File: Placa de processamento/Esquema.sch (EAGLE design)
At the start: 14 parts

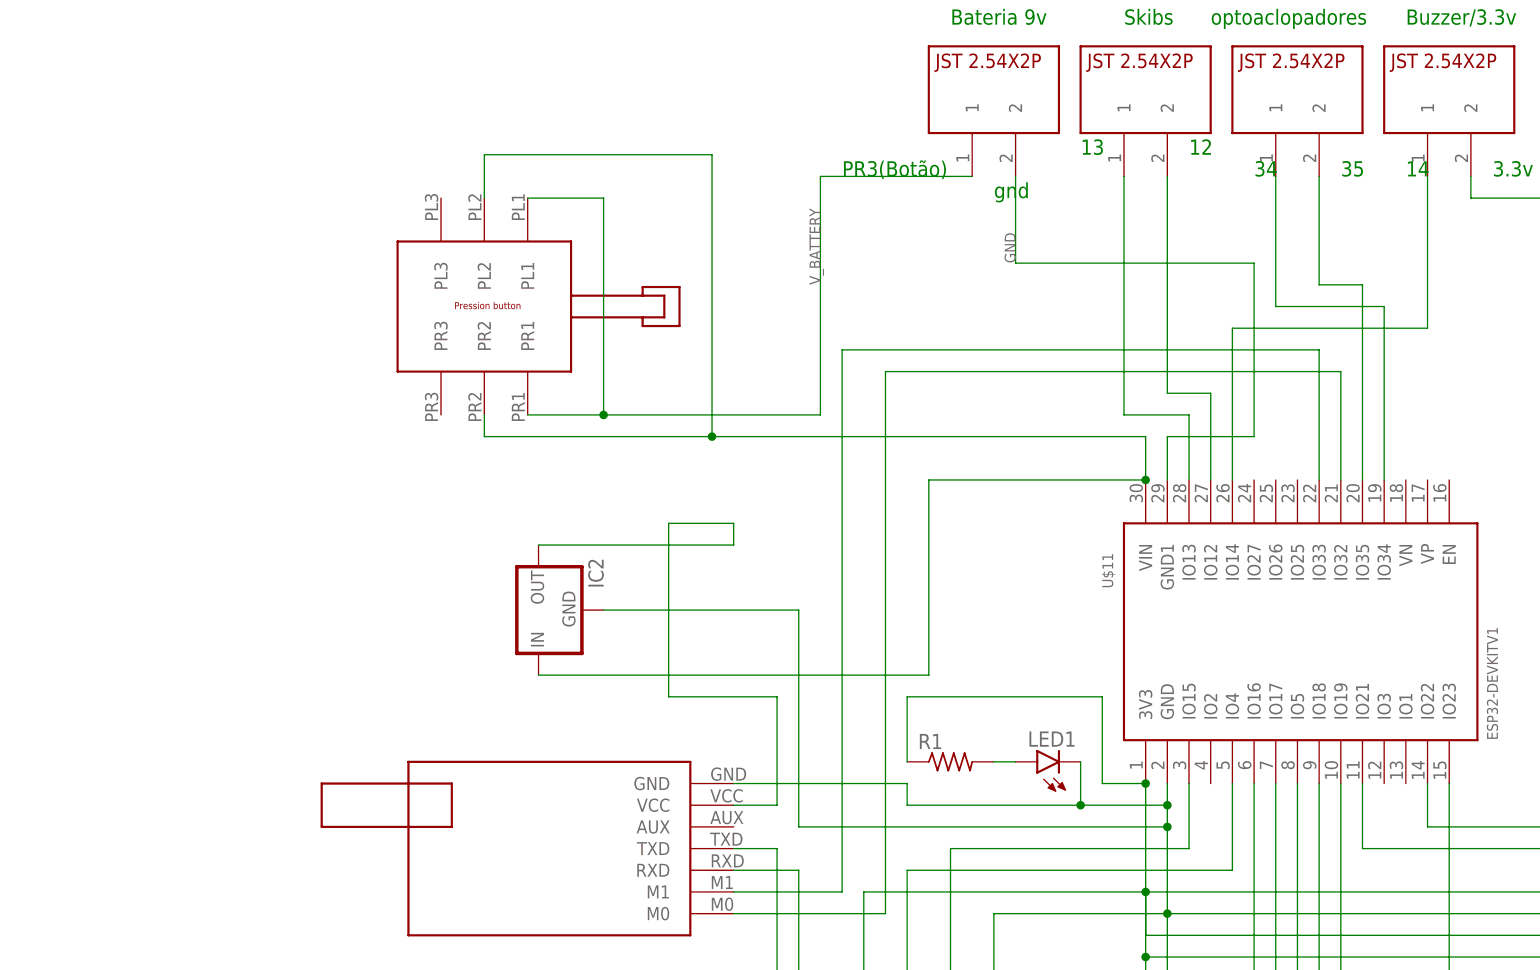
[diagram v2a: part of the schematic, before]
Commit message: Adiciona Placa de processamento ao repositório
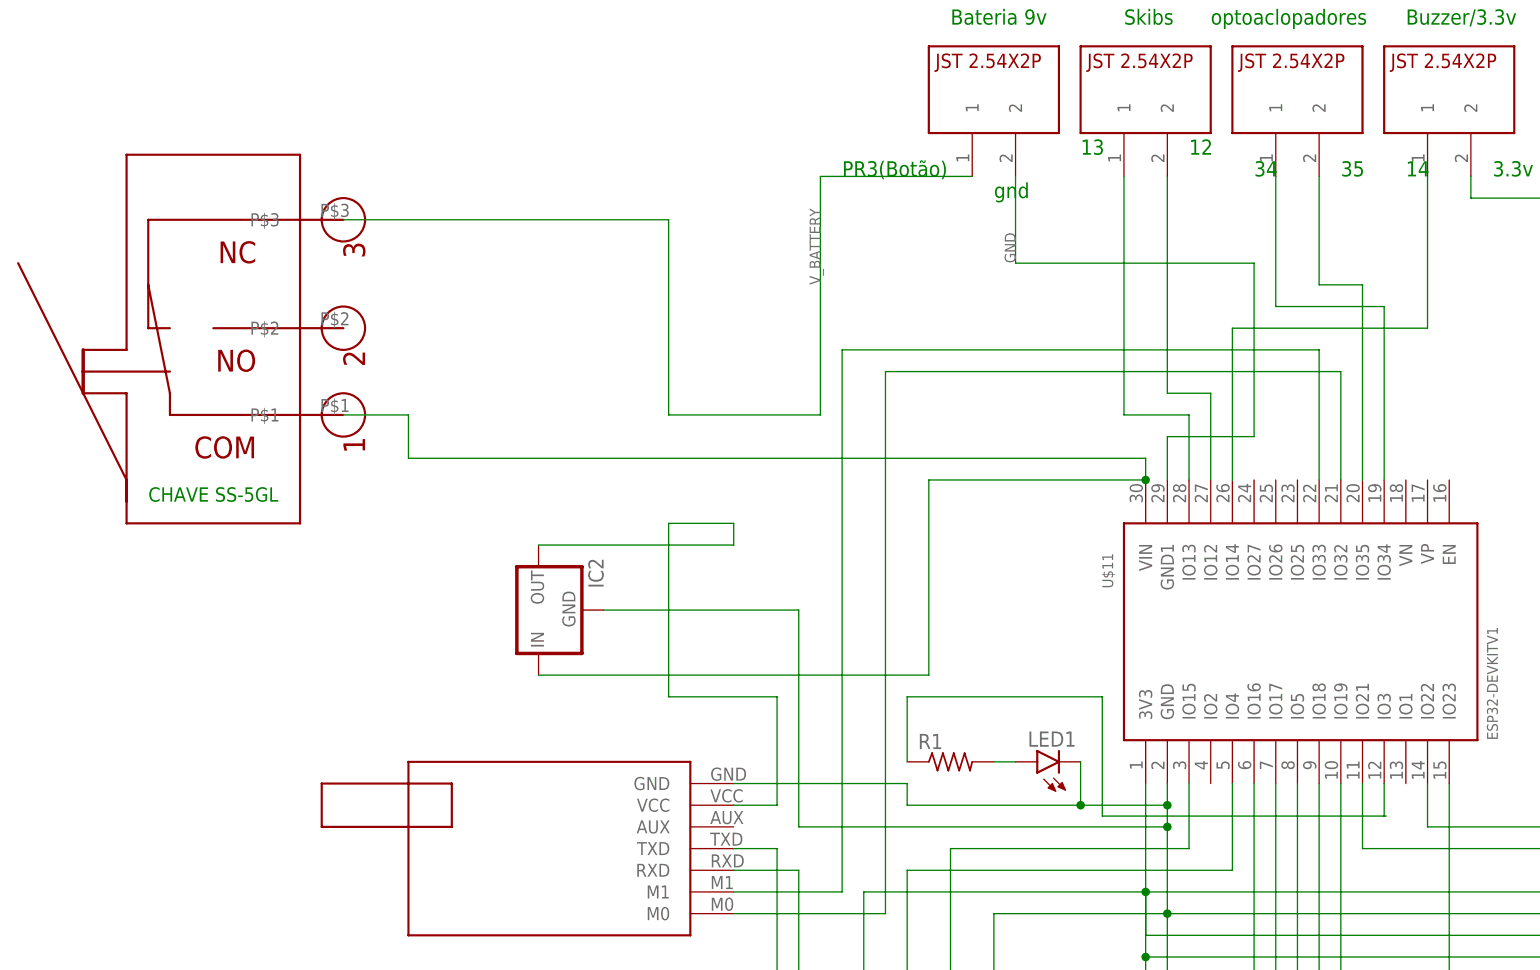
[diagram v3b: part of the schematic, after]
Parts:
- removed U$10: PRESSION_BUTTON, CRD:PRESSION_BUTTON
- added U$12: CHAVE_SS-5GL, CRD:CHAVE_SS-5GL
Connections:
- new net N$17: R1.1, U$11.IO3
- net N$3: no longer R1.1
- net N$7: now also U$12.P$1; no longer U$10.PL2, U$10.PR2
- net V_BATTERY: now also U$12.P$3; no longer U$10.PL1, U$10.PR1
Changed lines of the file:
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@@
 <parts>
 <part name="U$1" library="CRD" library_urn="urn:adsk.eagle:library:39051337" deviceset="BMP390" device="V1" package3d_urn="urn:adsk.eagle:package:40965124/5"/>
-<part name="U$2" library="CRD" library_urn="urn:adsk.eagle:library:39051337" deviceset="E22-400T30D" device="" package3d_urn="urn:adsk.eagle:package:40965099/4"/>
-<part name="U$3" library="CRD" library_urn="urn:adsk.eagle:library:39051337" deviceset="GPS_MODULE" device="" package3d_urn="urn:adsk.eagle:package:39608400/5"/>
+<part name="U$2" library="CRD" library_urn="urn:adsk.eagle:library:39051337" deviceset="E22-400T30D" device="" package3d_urn="urn:adsk.eagle:package:40965099/5"/>
+<part name="U$3" library="CRD" library_urn="urn:adsk.eagle:library:39051337" deviceset="GPS_MODULE" device="" package3d_urn="urn:adsk.eagle:package:39608400/7"/>
 <part name="U$4" library="CRD" library_urn="urn:adsk.eagle:library:39051337" deviceset="JST2.54X2P" device="" package3d_urn="urn:adsk.eagle:package:39191967/2"/>
 <part name="U$5" library="CRD" library_urn="urn:adsk.eagle:library:39051337" deviceset="JST2.54X2P" device="" package3d_urn="urn:adsk.eagle:package:39191967/2"/>
 <part name="U$6" library="CRD" library_urn="urn:adsk.eagle:library:39051337" deviceset="JST2.54X2P" device="" package3d_urn="urn:adsk.eagle:package:39191967/2"/>
 <part name="U$7" library="CRD" library_urn="urn:adsk.eagle:library:39051337" deviceset="JST2.54X2P" device="" package3d_urn="urn:adsk.eagle:package:39191967/2"/>
-<part name="U$10" library="CRD" library_urn="urn:adsk.eagle:library:39051337" deviceset="PRESSION_BUTTON" device="" package3d_urn="urn:adsk.eagle:package:43483815/3"/>
 <part name="U$8" library="CRD" library_urn="urn:adsk.eagle:library:39051337" deviceset="MICROSD_SMALL_READER" device="" package3d_urn="urn:adsk.eagle:package:44017969/2"/>
 <part name="U$9" library="CRD" library_urn="urn:adsk.eagle:library:39051337" deviceset="MPU6050" device="V1" package3d_urn="urn:adsk.eagle:package:39029071/8"/>
@@
 <part name="LED1" library="led" library_urn="urn:adsk.eagle:library:259" deviceset="LED" device="5MM" package3d_urn="urn:adsk.eagle:package:15799/2"/>
 <part name="R1" library="rcl" library_urn="urn:adsk.eagle:library:334" deviceset="R-US_" device="0309/12" package3d_urn="urn:adsk.eagle:package:23571/1"/>
+<part name="U$12" library="CRD" library_urn="urn:adsk.eagle:library:39051337" deviceset="CHAVE_SS-5GL" device="" package3d_urn="urn:adsk.eagle:package:45208058/6"/>
 </parts>
 <sheets>
@@
 <instances>
 <instance part="U$1" gate="G$1" x="144.78" y="60.96" smashed="yes"/>
-<instance part="U$2" gate="G$1" x="-22.86" y="-7.62" smashed="yes" rot="R180"/>
+<instance part="U$2" gate="LORA_E22400T30D" x="-22.86" y="-7.62" smashed="yes" rot="R180"/>
 <instance part="U$3" gate="G$1" x="22.86" y="-50.8" smashed="yes" rot="R180"/>
 <instance part="U$4" gate="G$1" x="83.82" y="81.28" smashed="yes"/>
@@
 <instance part="U$6" gate="G$1" x="48.26" y="81.28" smashed="yes"/>
 <instance part="U$7" gate="G$1" x="30.48" y="81.28" smashed="yes"/>
-<instance part="U$10" gate="G$1" x="-20.32" y="55.88" smashed="yes" rot="R180"/>
 <instance part="U$8" gate="G$1" x="152.4" y="-58.42" smashed="yes"/>
 <instance part="U$9" gate="G$1" x="190.5" y="60.96" smashed="yes"/>
@@
 <attribute name="VALUE" x="21.59" y="-0.762" size="1.778" layer="96"/>
 </instance>
+<instance part="U$12" gate="G$1" x="-58.42" y="53.34" smashed="yes" rot="R90"/>
 </instances>
 <busses>
@@
 <wire x1="119.38" y1="-20.32" x2="48.26" y2="-20.32" width="0.1524" layer="91"/>
 <junction x="48.26" y="-20.32"/>
-<pinref part="R1" gate="G$1" pin="1"/>
-<wire x1="20.32" y1="2.54" x2="20.32" y2="10.16" width="0.1524" layer="91"/>
-<wire x1="20.32" y1="10.16" x2="43.18" y2="10.16" width="0.1524" layer="91"/>
-<wire x1="43.18" y1="10.16" x2="43.18" y2="0" width="0.1524" layer="91"/>
-<wire x1="43.18" y1="0" x2="48.26" y2="0" width="0.1524" layer="91"/>
-<junction x="48.26" y="0"/>
 </segment>
 </net>
@@
 <pinref part="U$11" gate="G$1" pin="IO17"/>
 <wire x1="63.5" y1="-22.86" x2="63.5" y2="0" width="0.1524" layer="91"/>
-<pinref part="U$2" gate="G$1" pin="RXD"/>
+<pinref part="U$2" gate="LORA_E22400T30D" pin="RXD"/>
 <wire x1="7.62" y1="-10.16" x2="0" y2="-10.16" width="0.1524" layer="91"/>
 </segment>
@@
 <wire x1="5.08" y1="-25.4" x2="60.96" y2="-25.4" width="0.1524" layer="91"/>
 <wire x1="60.96" y1="-25.4" x2="60.96" y2="0" width="0.1524" layer="91"/>
-<pinref part="U$2" gate="G$1" pin="TXD"/>
+<pinref part="U$2" gate="LORA_E22400T30D" pin="TXD"/>
 <wire x1="5.08" y1="-7.62" x2="0" y2="-7.62" width="0.1524" layer="91"/>
 </segment>
@@
 <net name="N$10" class="0">
 <segment>
-<pinref part="U$2" gate="G$1" pin="M1"/>
+<pinref part="U$2" gate="LORA_E22400T30D" pin="M1"/>
 <wire x1="0" y1="-12.7" x2="12.7" y2="-12.7" width="0.1524" layer="91"/>
 <wire x1="12.7" y1="-12.7" x2="12.7" y2="50.8" width="0.1524" layer="91"/>
@@
 <net name="N$11" class="0">
 <segment>
-<pinref part="U$2" gate="G$1" pin="M0"/>
+<pinref part="U$2" gate="LORA_E22400T30D" pin="M0"/>
 <wire x1="0" y1="-15.24" x2="17.78" y2="-15.24" width="0.1524" layer="91"/>
 <wire x1="17.78" y1="-15.24" x2="17.78" y2="48.26" width="0.1524" layer="91"/>
@@
 <segment>
 <pinref part="U$11" gate="G$1" pin="VIN"/>
-<wire x1="-2.54" y1="40.64" x2="48.26" y2="40.64" width="0.1524" layer="91"/>
 <wire x1="22.86" y1="35.56" x2="48.26" y2="35.56" width="0.1524" layer="91"/>
 <wire x1="22.86" y1="12.7" x2="22.86" y2="35.56" width="0.1524" layer="91"/>
-<wire x1="48.26" y1="40.64" x2="48.26" y2="35.56" width="0.1524" layer="91"/>
-<junction x="48.26" y="35.56"/>
-<pinref part="U$10" gate="G$1" pin="PR2"/>
-<wire x1="-2.54" y1="73.66" x2="-2.54" y2="40.64" width="0.1524" layer="91"/>
-<wire x1="-29.21" y1="43.18" x2="-29.21" y2="40.64" width="0.1524" layer="91"/>
-<wire x1="-29.21" y1="40.64" x2="-2.54" y2="40.64" width="0.1524" layer="91"/>
-<junction x="-2.54" y="40.64"/>
-<pinref part="U$10" gate="G$1" pin="PL2"/>
-<wire x1="-29.21" y1="68.58" x2="-29.21" y2="73.66" width="0.1524" layer="91"/>
-<wire x1="-29.21" y1="73.66" x2="-2.54" y2="73.66" width="0.1524" layer="91"/>
 <pinref part="IC2" gate="A" pin="IN"/>
 <wire x1="22.86" y1="12.7" x2="-22.86" y2="12.7" width="0.1524" layer="91"/>
+<pinref part="U$12" gate="G$1" pin="P$1"/>
+<wire x1="-45.72" y1="43.18" x2="-38.1" y2="43.18" width="0.1524" layer="91"/>
+<wire x1="-38.1" y1="43.18" x2="-38.1" y2="38.1" width="0.1524" layer="91"/>
+<wire x1="-38.1" y1="38.1" x2="48.26" y2="38.1" width="0.1524" layer="91"/>
+<wire x1="48.26" y1="38.1" x2="48.26" y2="35.56" width="0.1524" layer="91"/>
+<junction x="48.26" y="35.56"/>
 </segment>
 </net>
@@
 <wire x1="-7.62" y1="30.48" x2="-7.62" y2="10.16" width="0.1524" layer="91"/>
 <wire x1="-7.62" y1="10.16" x2="5.08" y2="10.16" width="0.1524" layer="91"/>
-<pinref part="U$2" gate="G$1" pin="VCC"/>
+<pinref part="U$2" gate="LORA_E22400T30D" pin="VCC"/>
 <wire x1="5.08" y1="10.16" x2="5.08" y2="-2.54" width="0.1524" layer="91"/>
 <wire x1="5.08" y1="-2.54" x2="0" y2="-2.54" width="0.1524" layer="91"/>
@@
 <wire x1="10.16" y1="71.12" x2="27.94" y2="71.12" width="0.1524" layer="91"/>
 <label x="10.16" y="58.42" size="1.27" layer="95" rot="R90"/>
-<pinref part="U$10" gate="G$1" pin="PR1"/>
-<wire x1="-24.13" y1="43.18" x2="-15.24" y2="43.18" width="0.1524" layer="91"/>
-<wire x1="-15.24" y1="43.18" x2="-15.24" y2="68.58" width="0.1524" layer="91"/>
-<pinref part="U$10" gate="G$1" pin="PL1"/>
-<wire x1="-15.24" y1="68.58" x2="-24.13" y2="68.58" width="0.1524" layer="91"/>
-<wire x1="-15.24" y1="43.18" x2="10.16" y2="43.18" width="0.1524" layer="91"/>
-<junction x="-15.24" y="43.18"/>
+<pinref part="U$12" gate="G$1" pin="P$3"/>
+<wire x1="-45.72" y1="66.04" x2="-7.62" y2="66.04" width="0.1524" layer="91"/>
+<wire x1="-7.62" y1="66.04" x2="-7.62" y2="43.18" width="0.1524" layer="91"/>
+<wire x1="-7.62" y1="43.18" x2="10.16" y2="43.18" width="0.1524" layer="91"/>
 </segment>
 </net>
@@
 <wire x1="147.32" y1="-53.34" x2="50.8" y2="-53.34" width="0.1524" layer="91"/>
 <wire x1="50.8" y1="-53.34" x2="50.8" y2="-15.24" width="0.1524" layer="91"/>
-<pinref part="U$2" gate="G$1" pin="GND"/>
+<pinref part="U$2" gate="LORA_E22400T30D" pin="GND"/>
 <wire x1="0" y1="0" x2="20.32" y2="0" width="0.1524" layer="91"/>
 <wire x1="20.32" y1="0" x2="20.32" y2="-2.54" width="0.1524" layer="91"/>
@@
 </segment>
 </net>
+<net name="N$17" class="0">
+<segment>
+<wire x1="43.18" y1="10.16" x2="43.18" y2="-3.81" width="0.1524" layer="91"/>
+<wire x1="20.32" y1="10.16" x2="43.18" y2="10.16" width="0.1524" layer="91"/>
+<pinref part="R1" gate="G$1" pin="1"/>
+<wire x1="20.32" y1="2.54" x2="20.32" y2="10.16" width="0.1524" layer="91"/>
+<wire x1="43.18" y1="-3.81" x2="76.2" y2="-3.81" width="0.1524" layer="91"/>
+<pinref part="U$11" gate="G$1" pin="IO3"/>
+<wire x1="76.454" y1="-3.81" x2="76.2" y2="-3.81" width="0.1524" layer="91"/>
+<wire x1="76.2" y1="-3.81" x2="76.2" y2="0" width="0.1524" layer="91"/>
+</segment>
+</net>

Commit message: Coisas
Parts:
- added R2: 40R, rcl:R-US_0309/12
- IC2: value (none) -> 5V
- LED1: value (none) -> RED
- R1: value (none) -> 220R
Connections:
- net N$1 renamed SDA
- net N$10 renamed M1
- net N$11 renamed M0
- net N$13 renamed CS
- net N$14 renamed MOSI
- net N$15 renamed CLK
- net N$16 renamed MISO
- net N$17 renamed LED1
- net N$19 renamed SKIB1
- net N$2 renamed SCL
- net N$20 renamed SKIB2
- net N$21 renamed BUZZER
- net N$3 renamed 3V3
- net N$5 renamed TX1
- net N$6 renamed RX1
- net N$8 renamed TX2
- net N$9 renamed RX2
- removed net N$12: IC2.OUT, U$2.VCC
- removed net N$22: U$11.IO34, U$5.1
- removed net N$23: U$11.IO35, U$5.2
- new net OPTOACOPLADOR1: U$11.IO35, U$5.1
- new net OPTOACOPLADOR2: U$11.IO34, U$5.2
- new net VIN: IC2.IN, U$12.P$1
- new net VOUT: IC2.OUT, U$11.VIN, U$2.VCC
- net GND: now also R2.1; no longer U$11.GND1, U$2.GND
- net N$7: now also R2.2, U$2.GND; no longer IC2.IN, U$11.VIN, U$12.P$1
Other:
- note removed: "3.3v"
- note removed: "PR3(Botão)"
- note removed: "gnd"
- moved on the sheet: IC2, LED1, R1, U$11
